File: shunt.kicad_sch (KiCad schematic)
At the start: 0 parts

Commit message: started on shunt
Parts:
- added U4, U7: MAX4238AUT/V+T, 21-0058I_MXM, symbol 2026-03-24_14-06-06:MAX4238AUT_V+T
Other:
- note added: "These are shunt amplifiers, but the symbol is funny"
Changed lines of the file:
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@@
 	(generator_version "10.0")
 	(paper "A4")
+	(text "These are shunt amplifiers, but the symbol is funny"
+		(exclude_from_sim no)
+		(at 107.95 45.72 0)
+		(effects
+			(font
+				(size 1.27 1.27)
+			)
+		)
+	)
+	(hierarchical_label "Shunt1-"
+		(shape input)
+		(at 58.42 66.675 180)
+		(effects
+			(font
+				(size 1.27 1.27)
+			)
+			(justify right)
+		)
+	)
+	(hierarchical_label "Shunt2-"
+		(shape input)
+		(at 53.34 107.95 180)
+		(effects
+			(font
+				(size 1.27 1.27)
+			)
+			(justify right)
+		)
+	)
+	(hierarchical_label "Shunt1+"
+		(shape input)
+		(at 58.42 58.42 180)
+		(effects
+			(font
+				(size 1.27 1.27)
+			)
+			(justify right)
+		)
+	)
+	(hierarchical_label "Shunt2+"
+		(shape input)
+		(at 53.34 100.965 180)
+		(effects
+			(font
+				(size 1.27 1.27)
+			)
+			(justify right)
+		)
+	)
+	(symbol
+		(lib_id "2026-03-24_14-06-06:MAX4238AUT_V+T")
+		(at 81.915 62.23 0)
+		(unit 1)
+		(body_style 1)
+		(exclude_from_sim no)
+		(in_bom yes)
+		(on_board yes)
+		(in_pos_files yes)
+		(dnp no)
+		(fields_autoplaced yes)
+		(property "Reference" "U4"
+			(at 102.235 52.705 0)
+			(show_name no)
+			(do_not_autoplace no)
+			(effects
+				(font
+					(size 1.524 1.524)
+				)
+			)
+		)
+		(property "Value" "MAX4238AUT/V+T"
+			(at 102.235 55.245 0)
+			(show_name no)
+			(do_not_autoplace no)
+			(effects
+				(font
+					(size 1.524 1.524)
+				)
+			)
+		)
+		(property "Footprint" "21-0058I_MXM"
+			(at 81.915 62.23 0)
+			(hide yes)
+			(show_name no)
+			(do_not_autoplace no)
+			(effects
+				(font
+					(size 1.27 1.27)
+					(italic yes)
+				)
+			)
+		)
+		(property "Datasheet" "MAX4238AUT/V+T"
+			(at 81.915 62.23 0)
+			(hide yes)
+			(show_name no)
+			(do_not_autoplace no)
+			(effects
+				(font
+					(size 1.27 1.27)
+					(italic yes)
+				)
+			)
+		)
+		(property "Description" ""
+			(at 81.915 62.23 0)
+			(hide yes)
+			(show_name no)
+			(do_not_autoplace no)
+			(effects
+				(font
+					(size 1.27 1.27)
+				)
+			)
+		)
+		(pin "6"
+		)
+		(pin "3"
+		)
+		(pin "1"
+		)
+		(pin "5"
+		)
+		(pin "4"
+		)
+		(pin "2"
+		)
+		(instances
+			(project "LV_DCDC"
+				(path "/ccad4640-78c7-423b-83df-3ec0b90aa2b3/31d4a71c-66fd-4b80-a697-70e62f2ea215"
+					(reference "U4")
+					(unit 1)
+				)
+			)
+		)
+	)
+	(symbol
+		(lib_id "2026-03-24_14-06-06:MAX4238AUT_V+T")
+		(at 82.55 102.235 0)
+		(unit 1)
+		(body_style 1)
+		(exclude_from_sim no)
+		(in_bom yes)
+		(on_board yes)
+		(in_pos_files yes)
+		(dnp no)
+		(fields_autoplaced yes)
+		(property "Reference" "U7"
+			(at 102.87 92.71 0)
+			(show_name no)
+			(do_not_autoplace no)
+			(effects
+				(font
+					(size 1.524 1.524)
+				)
+			)
+		)
+		(property "Value" "MAX4238AUT/V+T"
+			(at 102.87 95.25 0)
+			(show_name no)
+			(do_not_autoplace no)
+			(effects
+				(font
+					(size 1.524 1.524)
+				)
+			)
+		)
+		(property "Footprint" "21-0058I_MXM"
+			(at 82.55 102.235 0)
+			(hide yes)
+			(show_name no)
+			(do_not_autoplace no)
+			(effects
+				(font
+					(size 1.27 1.27)
+					(italic yes)
+				)
+			)
+		)
+		(property "Datasheet" "MAX4238AUT/V+T"
+			(at 82.55 102.235 0)
+			(hide yes)
+			(show_name no)
+			(do_not_autoplace no)
+			(effects
+				(font
+					(size 1.27 1.27)
+					(italic yes)
+				)
+			)
+		)
+		(property "Description" ""
+			(at 82.55 102.235 0)
+			(hide yes)
+			(show_name no)
+			(do_not_autoplace no)
+			(effects
+				(font
+					(size 1.27 1.27)
+				)
+			)
+		)
+		(pin "6"
+		)
+		(pin "3"
+		)
+		(pin "1"
+		)
+		(pin "5"
+		)
+		(pin "4"
+		)
+		(pin "2"
+		)
+		(instances
+			(project "LV_DCDC"
+				(path "/ccad4640-78c7-423b-83df-3ec0b90aa2b3/31d4a71c-66fd-4b80-a697-70e62f2ea215"
+					(reference "U7")
+					(unit 1)
+				)
+			)
+		)
+	)
 )

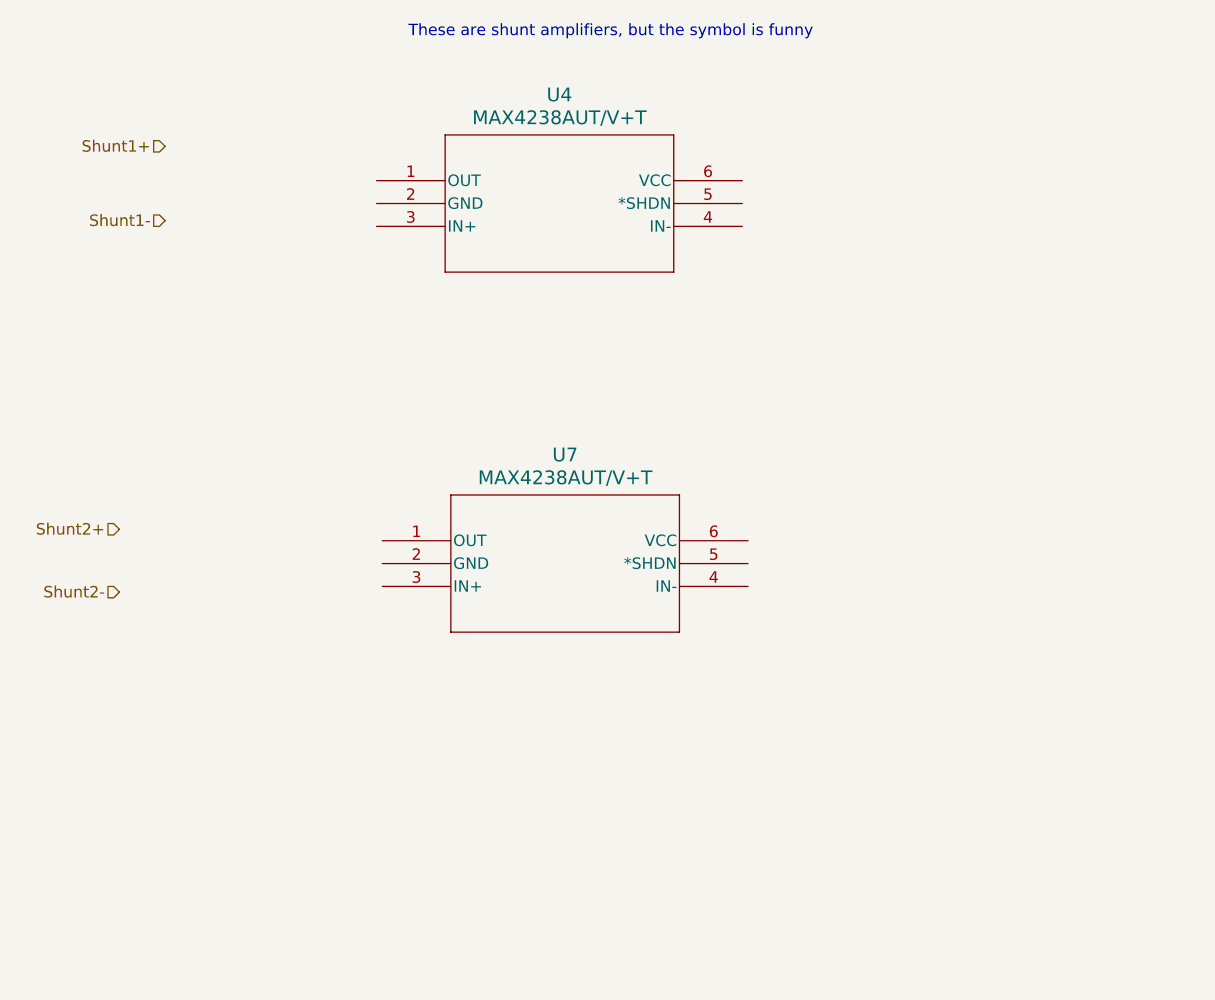
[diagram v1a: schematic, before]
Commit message: Made trim circuit
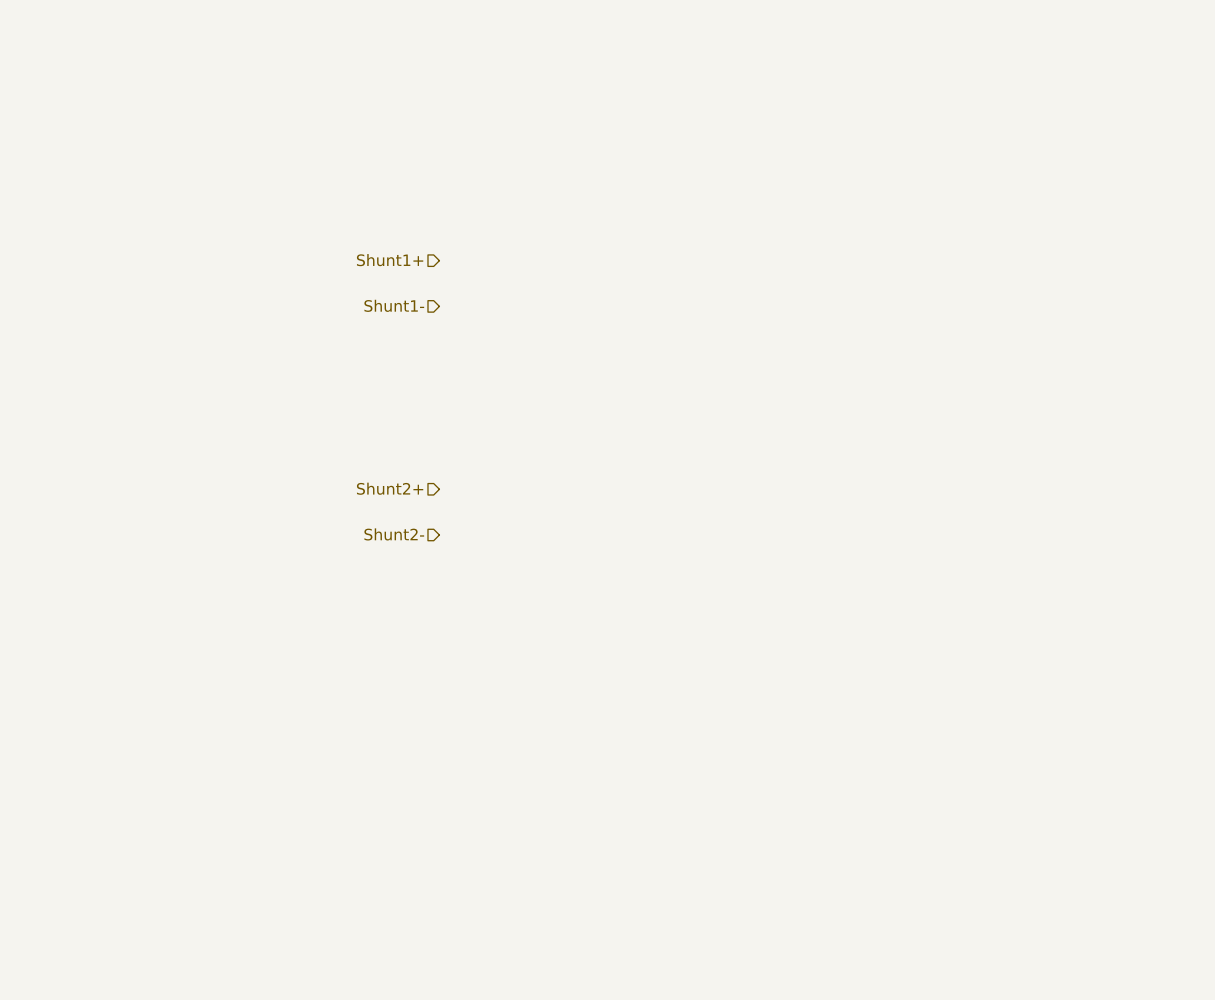
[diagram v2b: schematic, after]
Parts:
- removed U4, U7: MAX4238AUT/V+T, 21-0058I_MXM, symbol 2026-03-24_14-06-06:MAX4238AUT_V+T
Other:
- note removed: "These are shunt amplifiers, but the symbol is funny"
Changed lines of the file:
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@@
 	(generator_version "10.0")
 	(paper "A4")
-	(text "These are shunt amplifiers, but the symbol is funny"
-		(exclude_from_sim no)
-		(at 107.95 45.72 0)
-		(effects
-			(font
-				(size 1.27 1.27)
-			)
-		)
-	)
 	(hierarchical_label "Shunt1-"
 		(shape input)
-		(at 58.42 66.675 180)
+		(at 88.9 76.2 180)
 		(effects
 			(font
@@
 	(hierarchical_label "Shunt2-"
 		(shape input)
-		(at 53.34 107.95 180)
+		(at 88.9 101.6 180)
 		(effects
 			(font
@@
 	(hierarchical_label "Shunt1+"
 		(shape input)
-		(at 58.42 58.42 180)
+		(at 88.9 71.12 180)
 		(effects
 			(font
@@
 	(hierarchical_label "Shunt2+"
 		(shape input)
-		(at 53.34 100.965 180)
+		(at 88.9 96.52 180)
 		(effects
 			(font
@@
 		)
 	)
-	(symbol
-		(lib_id "2026-03-24_14-06-06:MAX4238AUT_V+T")
-		(at 81.915 62.23 0)
-		(unit 1)
-		(body_style 1)
-		(exclude_from_sim no)
-		(in_bom yes)
-		(on_board yes)
-		(in_pos_files yes)
-		(dnp no)
-		(fields_autoplaced yes)
-		(property "Reference" "U4"
-			(at 102.235 52.705 0)
-			(show_name no)
-			(do_not_autoplace no)
-			(effects
-				(font
-					(size 1.524 1.524)
-				)
-			)
-		)
-		(property "Value" "MAX4238AUT/V+T"
-			(at 102.235 55.245 0)
-			(show_name no)
-			(do_not_autoplace no)
-			(effects
-				(font
-					(size 1.524 1.524)
-				)
-			)
-		)
-		(property "Footprint" "21-0058I_MXM"
-			(at 81.915 62.23 0)
-			(hide yes)
-			(show_name no)
-			(do_not_autoplace no)
-			(effects
-				(font
-					(size 1.27 1.27)
-					(italic yes)
-				)
-			)
-		)
-		(property "Datasheet" "MAX4238AUT/V+T"
-			(at 81.915 62.23 0)
-			(hide yes)
-			(show_name no)
-			(do_not_autoplace no)
-			(effects
-				(font
-					(size 1.27 1.27)
-					(italic yes)
-				)
-			)
-		)
-		(property "Description" ""
-			(at 81.915 62.23 0)
-			(hide yes)
-			(show_name no)
-			(do_not_autoplace no)
-			(effects
-				(font
-					(size 1.27 1.27)
-				)
-			)
-		)
-		(pin "6"
-		)
-		(pin "3"
-		)
-		(pin "1"
-		)
-		(pin "5"
-		)
-		(pin "4"
-		)
-		(pin "2"
-		)
-		(instances
-			(project "LV_DCDC"
-				(path "/ccad4640-78c7-423b-83df-3ec0b90aa2b3/31d4a71c-66fd-4b80-a697-70e62f2ea215"
-					(reference "U4")
-					(unit 1)
-				)
-			)
-		)
-	)
-	(symbol
-		(lib_id "2026-03-24_14-06-06:MAX4238AUT_V+T")
-		(at 82.55 102.235 0)
-		(unit 1)
-		(body_style 1)
-		(exclude_from_sim no)
-		(in_bom yes)
-		(on_board yes)
-		(in_pos_files yes)
-		(dnp no)
-		(fields_autoplaced yes)
-		(property "Reference" "U7"
-			(at 102.87 92.71 0)
-			(show_name no)
-			(do_not_autoplace no)
-			(effects
-				(font
-					(size 1.524 1.524)
-				)
-			)
-		)
-		(property "Value" "MAX4238AUT/V+T"
-			(at 102.87 95.25 0)
-			(show_name no)
-			(do_not_autoplace no)
-			(effects
-				(font
-					(size 1.524 1.524)
-				)
-			)
-		)
-		(property "Footprint" "21-0058I_MXM"
-			(at 82.55 102.235 0)
-			(hide yes)
-			(show_name no)
-			(do_not_autoplace no)
-			(effects
-				(font
-					(size 1.27 1.27)
-					(italic yes)
-				)
-			)
-		)
-		(property "Datasheet" "MAX4238AUT/V+T"
-			(at 82.55 102.235 0)
-			(hide yes)
-			(show_name no)
-			(do_not_autoplace no)
-			(effects
-				(font
-					(size 1.27 1.27)
-					(italic yes)
-				)
-			)
-		)
-		(property "Description" ""
-			(at 82.55 102.235 0)
-			(hide yes)
-			(show_name no)
-			(do_not_autoplace no)
-			(effects
-				(font
-					(size 1.27 1.27)
-				)
-			)
-		)
-		(pin "6"
-		)
-		(pin "3"
-		)
-		(pin "1"
-		)
-		(pin "5"
-		)
-		(pin "4"
-		)
-		(pin "2"
-		)
-		(instances
-			(project "LV_DCDC"
-				(path "/ccad4640-78c7-423b-83df-3ec0b90aa2b3/31d4a71c-66fd-4b80-a697-70e62f2ea215"
-					(reference "U7")
-					(unit 1)
-				)
-			)
-		)
-	)

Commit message: added shunts
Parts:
- added C43, C44, C45, C46: 100nF, symbol Device:C
- added R27, R28: 1.1Mohm, symbol Device:R
- added R29, R30: 1kOhm, symbol Device:R
- added U11, U12: LMP8645HV, Package_TO_SOT_SMD:TSOT-23-6_HandSoldering, symbol HV-DCDC-rescue:LMP8645HV-HV_DCDC
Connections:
- net Shunt1+: now also U11.3 (+)
- net Shunt1-: now also U11.4 (-)
- net Shunt2+: now also U12.3 (+)
- net Shunt2-: now also U12.4 (-)
- new net: R27.1, U12.5 (RG)
- new net: R30.1, U11.1
- new net: R29.1, U12.1
- new net: R28.1, U11.5 (RG)
- new net +5V: C43.1, C44.1, U11.6 (V+), U12.6 (V+)
- new net CurrSense1: C46.1, R30.2
- new net CurrSense2: C45.1, R29.2
- new net GNDA: C43.2, C44.2, C45.2, C46.2, R27.2, R28.2, U11.2 (V-), U12.2 (V-)
